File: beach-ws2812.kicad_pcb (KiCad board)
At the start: 4 copper layers, 260 x 120 mm, 343 parts, among them CON101 BARREL_JACK, P101 CONN_01X03, SW101 Pushbutton, SW102 Pushbutton, U101 STM32F103C(8-B)Tx, U102 LM1117-3.3, U103 MAX811, X101 8MHz

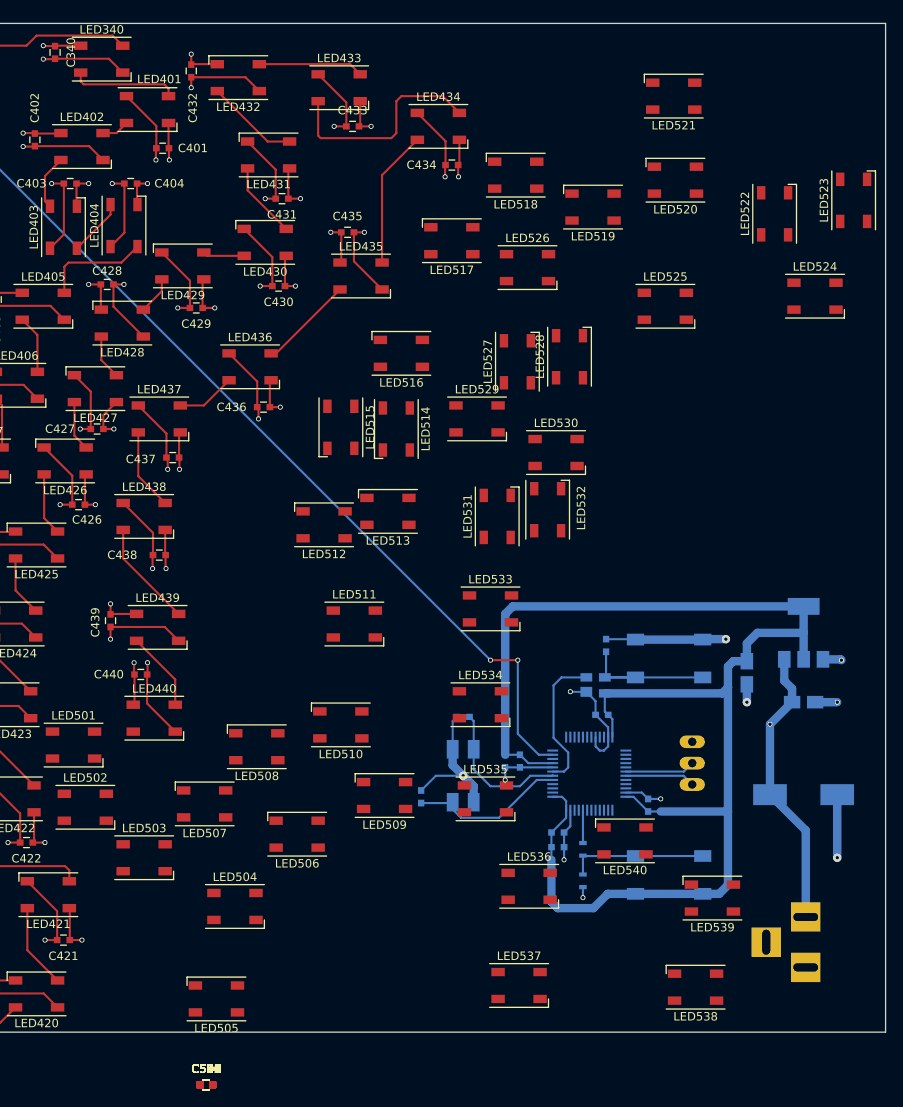
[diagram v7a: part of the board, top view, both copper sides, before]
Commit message: Routed 160 LEDs.
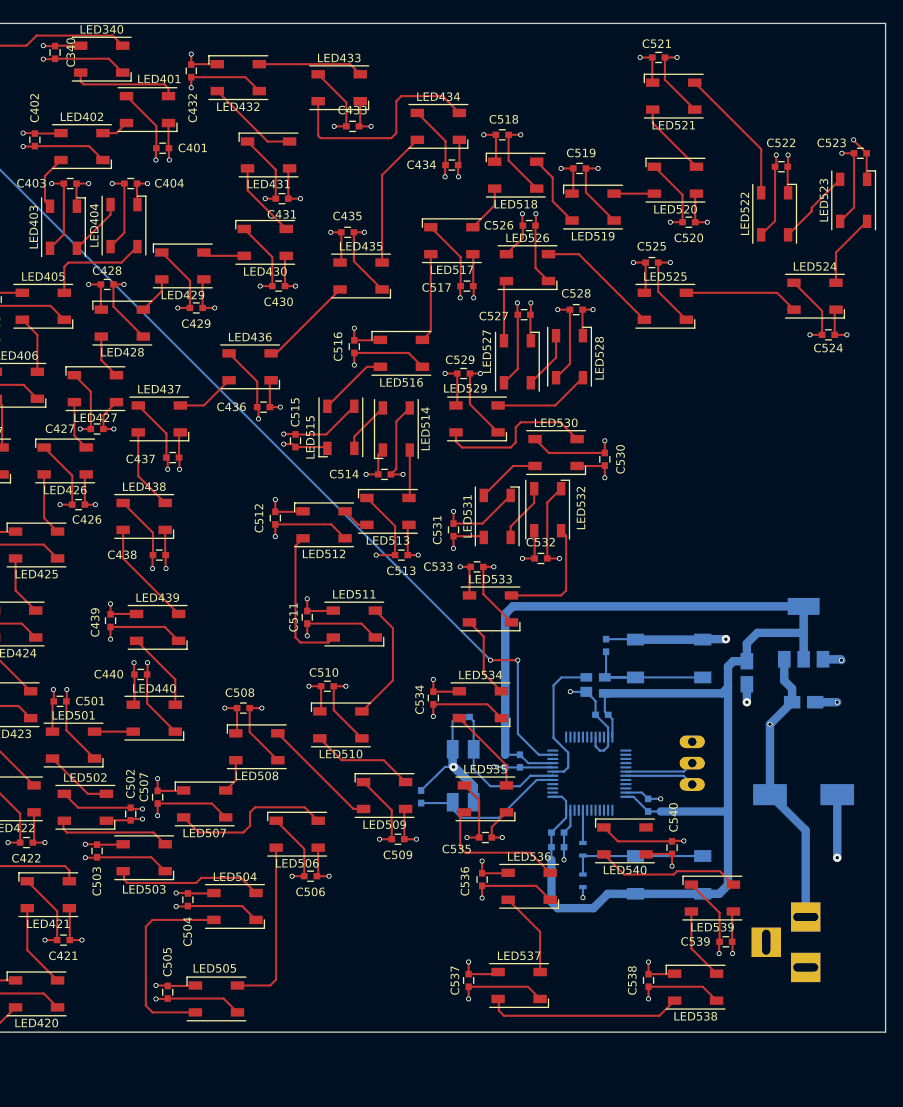
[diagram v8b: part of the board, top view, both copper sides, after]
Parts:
- moved C523 135.4 mm to (277.0, 34.2)
- moved C521 133.5 mm to (253.0, 22.8), turned to 180 degrees
- moved C522 128.9 mm to (267.6, 35.8)
- moved C518 118.4 mm to (234.4, 32.0), turned to 180 degrees
- moved C519 117.7 mm to (243.6, 36.0), turned to 180 degrees
- moved C520 117.6 mm to (256.6, 42.4), turned to 180 degrees
- moved C524 115.9 mm to (273.2, 55.8)
- moved C525 111.3 mm to (252.2, 47.2)
- moved C526 109.2 mm to (237.6, 42.8)
- moved C528 102.2 mm to (243.2, 52.8)
- moved C517 100.0 mm to (230.2, 50.0), turned to 180 degrees
- moved C527 99.1 mm to (237.0, 53.4)
- moved C529 90.0 mm to (229.8, 60.4)
- moved C516 89.6 mm to (216.8, 57.2), turned to 90 degrees
- moved C530 88.2 mm to (246.6, 70.6), turned to 270 degrees
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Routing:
- net +5V: track 962.5 -> 1265.2 mm, vias 121 -> 161
- net GND: track 1032.6 -> 1334.7 mm, vias 131 -> 171
- net Net-(LED504-Pad2): track 0.00 -> 24.1 mm
- net Net-(LED537-Pad2): track 0.00 -> 23.3 mm
- net Net-(LED505-Pad2): track 0.00 -> 20.6 mm
- net Net-(LED506-Pad2): track 0.00 -> 19.6 mm
- net Net-(LED529-Pad2): track 0.00 -> 18.9 mm
- net Net-(LED503-Pad2): track 0.00 -> 17.9 mm
- net Net-(LED539-Pad2): track 0.00 -> 17.2 mm
- net Net-(LED511-Pad2): track 0.00 -> 17.2 mm
- net Net-(LED521-Pad2): track 0.00 -> 16.4 mm
- net Net-(LED535-Pad2): track 0.00 -> 16.3 mm
- net Net-(LED525-Pad2): track 0.00 -> 14.6 mm
- net Net-(LED510-Pad2): track 0.00 -> 14.4 mm
- net Net-(LED532-Pad2): track 0.00 -> 14.1 mm
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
